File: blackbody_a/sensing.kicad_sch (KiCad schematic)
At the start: 3 parts, among them J1 Conn_02x03_Counter_Clockwise

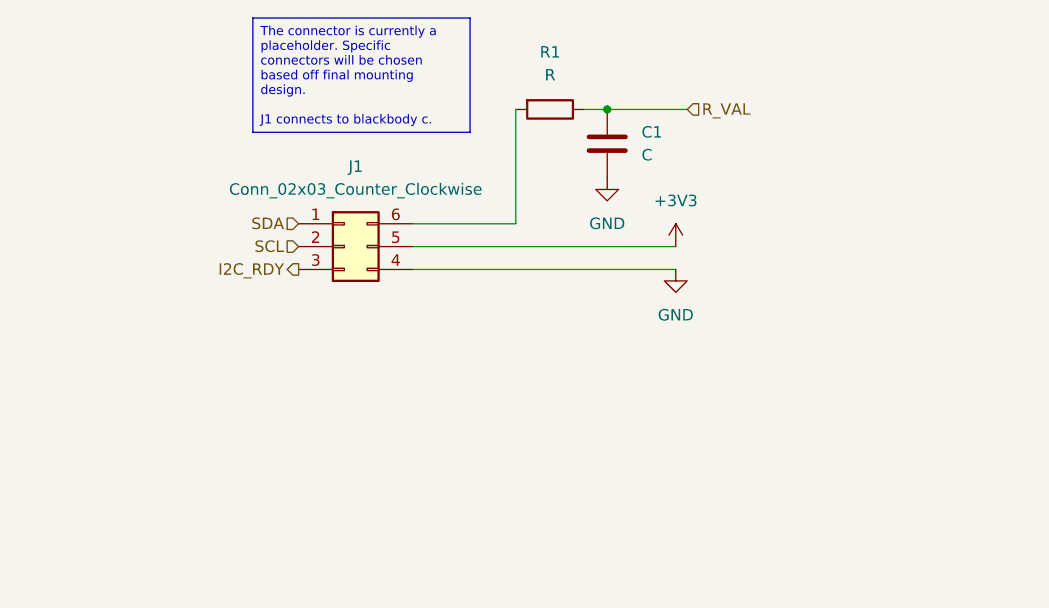
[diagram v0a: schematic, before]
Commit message: Initial version of sensor communication through all three boards
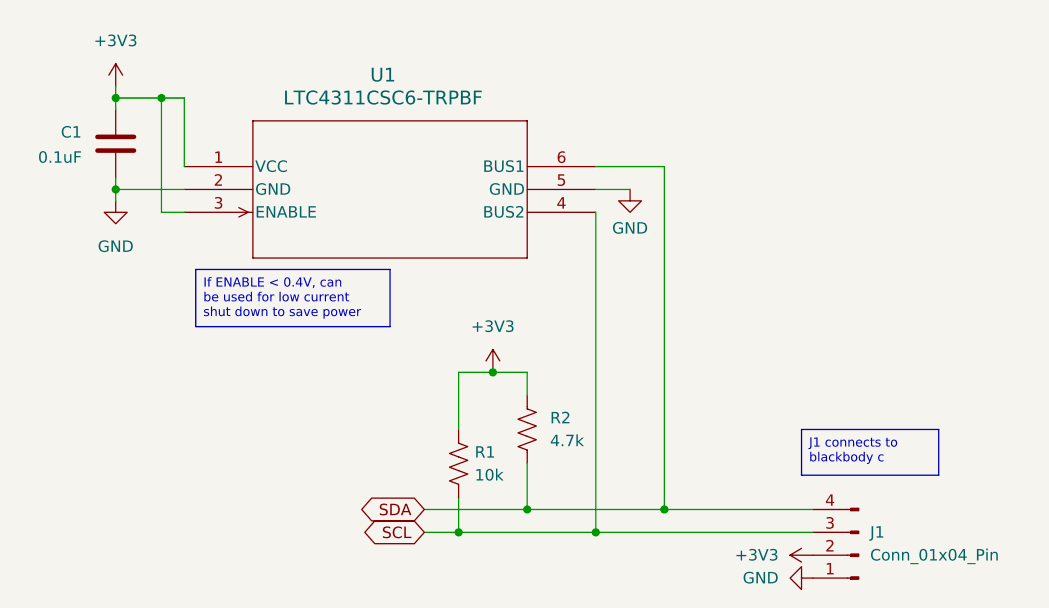
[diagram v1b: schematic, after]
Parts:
- removed J1: Conn_02x03_Counter_Clockwise, symbol Connector_Generic:Conn_02x03_Counter_Clockwise
- removed R1: R, symbol Device:R
- added J1: Conn_01x04_Pin, symbol Connector:Conn_01x04_Pin
- added R1: 10k, symbol Device:R_US
- added R2: 4.7k, symbol Device:R_US
- added U1: LTC4311CSC6-TRPBF, SOT-6_SC_LIT, symbol LTC4311:LTC4311CSC6-TRPBF
- C1: value C -> 0.1uF
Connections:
- net R_VAL is gone; now on net GND: C1.1
- net +3V3: now also C1.2, J1.2 (Pin_2), R1.1, R2.1, U1.1 (VCC), U1.3 (ENABLE)
- net GND: now also J1.1 (Pin_1), U1.2 (GND), U1.5 (GND); no longer C1.2
- net SCL: now also J1.3 (Pin_3), R1.2, U1.4 (BUS2)
- net SDA: now also J1.4 (Pin_4), R2.2, U1.6 (BUS1)

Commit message: Updated minor errors
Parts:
- R1: value 10k -> 4.7k
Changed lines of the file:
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@@
 			)
 		)
-		(property "Value" "10k"
+		(property "Value" "4.7k"
 			(at 116.078 93.98 0)
 			(effects

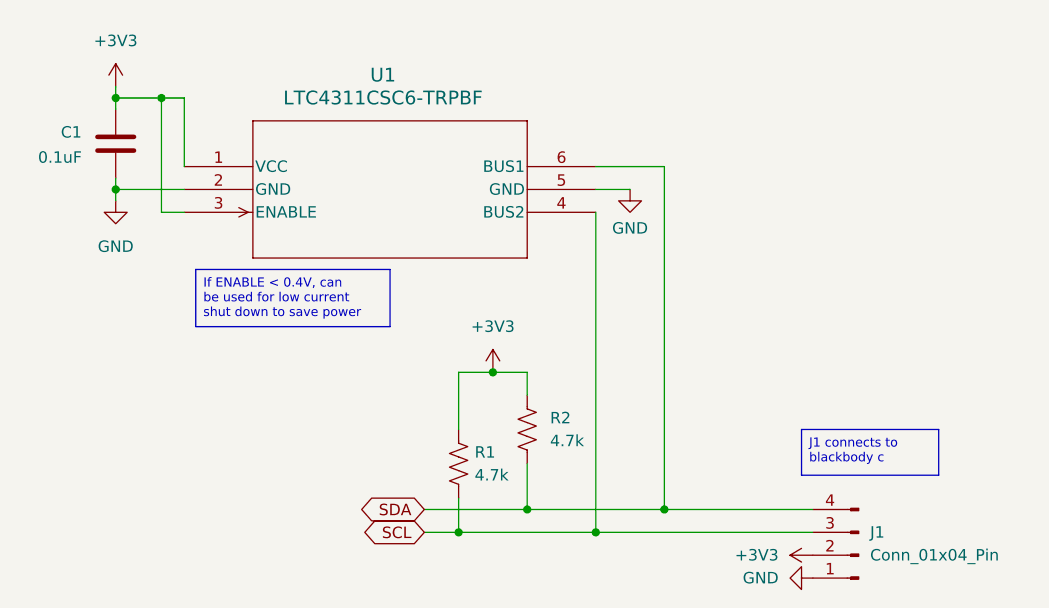
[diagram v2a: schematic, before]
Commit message: Added power distribution
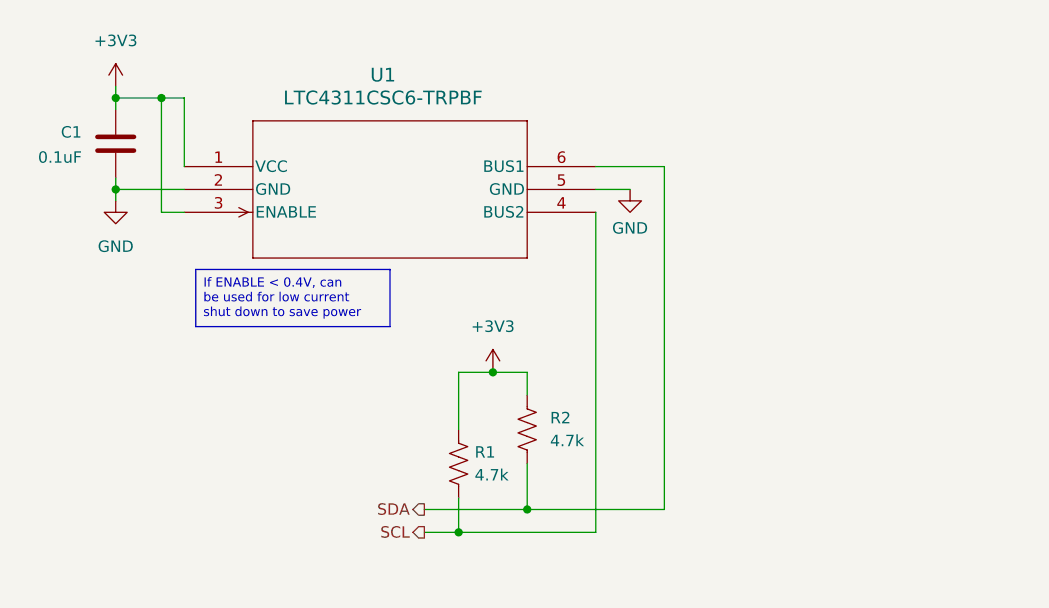
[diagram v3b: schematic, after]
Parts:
- removed J1: Conn_01x04_Pin, symbol Connector:Conn_01x04_Pin

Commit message: layout iteration 1
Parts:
- C1: footprint (none) -> Capacitor_SMD:C_0805_2012Metric
- R1, R2: footprint (none) -> Resistor_SMD:R_0805_2012Metric
- U1: footprint SOT-6_SC_LIT -> blackbody_a:SOT-6_SC_LIT
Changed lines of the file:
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@@
 (kicad_sch
-	(version 20231120)
+	(version 20250114)
 	(generator "eeschema")
-	(generator_version "8.0")
+	(generator_version "9.0")
 	(paper "A4")
+	(text_box "If ENABLE < 0.4V, can be used for low current shut down to save power"
+		(exclude_from_sim no)
+		(at 85.09 71.12 0)
+		(size 21.59 6.35)
+		(margins 0.762 0.762 0.762 0.762)
+		(stroke
+			(width 0)
+			(type default)
+		)
+		(fill
+			(type none)
+		)
+		(effects
+			(font
+				(size 1.016 1.016)
+			)
+			(justify left top)
+		)
+	)
 	(junction
 		(at 81.28 52.07)
@@
 		)
 	)
-	(text_box "If ENABLE < 0.4V, can be used for low current shut down to save power"
-		(exclude_from_sim no)
-		(at 85.09 71.12 0)
-		(size 21.59 6.35)
-		(stroke
-			(width 0)
-			(type default)
-		)
-		(fill
-			(type none)
-		)
-		(effects
-			(font
-				(size 1.016 1.016)
-			)
-			(justify left top)
-		)
-	)
 	(hierarchical_label "SCL"
 		(shape output)
 		(at 110.49 100.33 180)
-		(fields_autoplaced yes)
 		(effects
 			(font
@@
 		(shape output)
 		(at 110.49 97.79 180)
-		(fields_autoplaced yes)
 		(effects
 			(font
@@
 			)
 		)
-		(property "Footprint" ""
+		(property "Footprint" "Resistor_SMD:R_0805_2012Metric"
 			(at 115.316 92.964 90)
 			(effects
@@
 			)
 		)
-		(property "Footprint" "SOT-6_SC_LIT"
+		(property "Footprint" "blackbody_a:SOT-6_SC_LIT"
 			(at 83.82 59.69 0)
 			(effects
@@
 			)
 		)
-		(property "Footprint" ""
+		(property "Footprint" "Resistor_SMD:R_0805_2012Metric"
 			(at 122.936 89.154 90)
 			(effects
@@
 			)
 		)
-		(property "Footprint" ""
+		(property "Footprint" "Capacitor_SMD:C_0805_2012Metric"
 			(at 75.2348 53.34 0)
 			(effects

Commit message: layout edits
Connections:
- net +3V3 renamed +3.3V
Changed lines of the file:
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@@
+	)
+	(junction
+		(at 118.11 82.55)
+		(diameter 0)
+		(color 0 0 0 0)
 	)
 	(junction
@@
 		(color 0 0 0 0)
 	)
-	(junction
-		(at 118.11 82.55)
-		(diameter 0)
-		(color 0 0 0 0)
-	)
 	(wire
 		(pts
@@
 	(wire
 		(pts
+			(xy 81.28 64.77) (xy 81.28 52.07)
+		)
+		(stroke
+			(width 0)
+			(type default)
+		)
+	)
+	(wire
+		(pts
+			(xy 110.49 100.33) (xy 114.3 100.33)
+		)
+		(stroke
+			(width 0)
+			(type default)
+		)
+	)
+	(wire
+		(pts
+			(xy 121.92 82.55) (xy 121.92 85.09)
+		)
+		(stroke
+			(width 0)
+			(type default)
+		)
+	)
+	(wire
+		(pts
+			(xy 129.54 59.69) (xy 137.16 59.69)
+		)
+		(stroke
+			(width 0)
+			(type default)
+		)
+	)
+	(wire
+		(pts
+			(xy 76.2 52.07) (xy 76.2 53.34)
+		)
+		(stroke
+			(width 0)
+			(type default)
+		)
+	)
+	(wire
+		(pts
+			(xy 83.82 64.77) (xy 81.28 64.77)
+		)
+		(stroke
+			(width 0)
+			(type default)
+		)
+	)
+	(wire
+		(pts
+			(xy 137.16 59.69) (xy 137.16 97.79)
+		)
+		(stroke
+			(width 0)
+			(type default)
+		)
+	)
+	(wire
+		(pts
+			(xy 76.2 52.07) (xy 81.28 52.07)
+		)
+		(stroke
+			(width 0)
+			(type default)
+		)
+	)
+	(wire
+		(pts
+			(xy 114.3 82.55) (xy 118.11 82.55)
+		)
+		(stroke
+			(width 0)
+			(type default)
+		)
+	)
+	(wire
+		(pts
+			(xy 83.82 52.07) (xy 83.82 59.69)
+		)
+		(stroke
+			(width 0)
+			(type default)
+		)
+	)
+	(wire
+		(pts
+			(xy 76.2 62.23) (xy 83.82 62.23)
+		)
+		(stroke
+			(width 0)
+			(type default)
+		)
+	)
+	(wire
+		(pts
+			(xy 114.3 100.33) (xy 129.54 100.33)
+		)
+		(stroke
+			(width 0)
+			(type default)
+		)
+	)
+	(wire
+		(pts
+			(xy 81.28 52.07) (xy 83.82 52.07)
+		)
+		(stroke
+			(width 0)
+			(type default)
+		)
+	)
+	(wire
+		(pts
+			(xy 121.92 92.71) (xy 121.92 97.79)
+		)
+		(stroke
+			(width 0)
+			(type default)
+		)
+	)
+	(wire
+		(pts
 			(xy 118.11 82.55) (xy 121.92 82.55)
-		)
-		(stroke
-			(width 0)
-			(type default)
-		)
-	)
-	(wire
-		(pts
-			(xy 81.28 64.77) (xy 81.28 52.07)
-		)
-		(stroke
-			(width 0)
-			(type default)
-		)
-	)
-	(wire
-		(pts
-			(xy 110.49 100.33) (xy 114.3 100.33)
-		)
-		(stroke
-			(width 0)
-			(type default)
-		)
-	)
-	(wire
-		(pts
-			(xy 121.92 82.55) (xy 121.92 85.09)
-		)
-		(stroke
-			(width 0)
-			(type default)
-		)
-	)
-	(wire
-		(pts
-			(xy 129.54 59.69) (xy 137.16 59.69)
-		)
-		(stroke
-			(width 0)
-			(type default)
-		)
-	)
-	(wire
-		(pts
-			(xy 76.2 52.07) (xy 76.2 53.34)
-		)
-		(stroke
-			(width 0)
-			(type default)
-		)
-	)
-	(wire
-		(pts
-			(xy 83.82 64.77) (xy 81.28 64.77)
-		)
-		(stroke
-			(width 0)
-			(type default)
-		)
-	)
-	(wire
-		(pts
-			(xy 137.16 59.69) (xy 137.16 97.79)
-		)
-		(stroke
-			(width 0)
-			(type default)
-		)
-	)
-	(wire
-		(pts
-			(xy 76.2 52.07) (xy 81.28 52.07)
-		)
-		(stroke
-			(width 0)
-			(type default)
-		)
-	)
-	(wire
-		(pts
-			(xy 114.3 82.55) (xy 118.11 82.55)
-		)
-		(stroke
-			(width 0)
-			(type default)
-		)
-	)
-	(wire
-		(pts
-			(xy 83.82 52.07) (xy 83.82 59.69)
-		)
-		(stroke
-			(width 0)
-			(type default)
-		)
-	)
-	(wire
-		(pts
-			(xy 76.2 62.23) (xy 83.82 62.23)
-		)
-		(stroke
-			(width 0)
-			(type default)
-		)
-	)
-	(wire
-		(pts
-			(xy 114.3 100.33) (xy 129.54 100.33)
-		)
-		(stroke
-			(width 0)
-			(type default)
-		)
-	)
-	(wire
-		(pts
-			(xy 81.28 52.07) (xy 83.82 52.07)
-		)
-		(stroke
-			(width 0)
-			(type default)
-		)
-	)
-	(wire
-		(pts
-			(xy 121.92 92.71) (xy 121.92 97.79)
 		)
 		(stroke
@@
 	)
 	(symbol
-		(lib_id "power:+3V3")
-		(at 76.2 50.8 0)
-		(unit 1)
-		(exclude_from_sim no)
-		(in_bom yes)
-		(on_board yes)
-		(dnp no)
-		(fields_autoplaced yes)
-		(property "Reference" "#PWR02"
-			(at 76.2 54.61 0)
-			(effects
-				(font
-					(size 1.27 1.27)
-				)
-				(hide yes)
-			)
-		)
-		(property "Value" "+3V3"
-			(at 76.2 45.72 0)
-			(effects
-				(font
-					(size 1.27 1.27)
-				)
-			)
-		)
-		(property "Footprint" ""
-			(at 76.2 50.8 0)
-			(effects
-				(font
-					(size 1.27 1.27)
-				)
-				(hide yes)
-			)
-		)
-		(property "Datasheet" ""
-			(at 76.2 50.8 0)
-			(effects
-				(font
-					(size 1.27 1.27)
-				)
-				(hide yes)
-			)
-		)
-		(property "Description" "Power symbol creates a global label with name \"+3V3\""
-			(at 76.2 50.8 0)
-			(effects
-				(font
-					(size 1.27 1.27)
-				)
-				(hide yes)
-			)
-		)
-		(pin "1"
-		)
-		(instances
-			(project "blackbody_a"
-				(path "/1fc8ae43-742a-46b6-a93b-79253d0d0202/23416f09-d335-4c4f-b453-076ae86ec0b4"
-					(reference "#PWR02")
-					(unit 1)
-				)
-			)
-		)
-	)
-	(symbol
 		(lib_id "power:GND")
 		(at 133.35 62.23 0)
@@
 	)
 	(symbol
-		(lib_id "power:+3V3")
+		(lib_id "power:+3.3V")
 		(at 118.11 82.55 0)
 		(unit 1)
@@
 		(dnp no)
 		(fields_autoplaced yes)
-		(property "Reference" "#PWR04"
+		(property "Reference" "#PWR035"
 			(at 118.11 86.36 0)
 			(effects
@@
 			)
 		)
-		(property "Value" "+3V3"
+		(property "Value" "+3.3V"
 			(at 118.11 77.47 0)
 			(effects
@@
 			)
 		)
-		(property "Description" "Power symbol creates a global label with name \"+3V3\""
+		(property "Description" "Power symbol creates a global label with name \"+3.3V\""
 			(at 118.11 82.55 0)
 			(effects
@@
 			(project "blackbody_a"
 				(path "/1fc8ae43-742a-46b6-a93b-79253d0d0202/23416f09-d335-4c4f-b453-076ae86ec0b4"
-					(reference "#PWR04")
+					(reference "#PWR035")
 					(unit 1)
 				)
@@
 					(unit 1)
 				)
+			)
+		)
+	)
+	(symbol
+		(lib_id "power:+3.3V")
+		(at 76.2 50.8 0)
+		(unit 1)
+		(exclude_from_sim no)
+		(in_bom yes)
+		(on_board yes)
+		(dnp no)
+		(fields_autoplaced yes)
+		(property "Reference" "#PWR040"
+			(at 76.2 54.61 0)
+			(effects
+				(font
+					(size 1.27 1.27)
+				)
+				(hide yes)
+			)
+		)
+		(property "Value" "+3.3V"
+			(at 76.2 45.72 0)
+			(effects
+				(font
+					(size 1.27 1.27)
+				)
+			)
+		)
+		(property "Footprint" ""
+			(at 76.2 50.8 0)
+			(effects
+				(font
+					(size 1.27 1.27)
+				)
+				(hide yes)
+			)
+		)
+		(property "Datasheet" ""
+			(at 76.2 50.8 0)
+			(effects
+				(font
+					(size 1.27 1.27)
+				)
+				(hide yes)
+			)
+		)
+		(property "Description" "Power symbol creates a global label with name \"+3.3V\""
+			(at 76.2 50.8 0)
+			(effects
+				(font
+					(size 1.27 1.27)
+				)
+				(hide yes)
+			)
+		)
+		(pin "1"
+		)
+		(instances
+			(project "blackbody_a"
+				(path "/1fc8ae43-742a-46b6-a93b-79253d0d0202/23416f09-d335-4c4f-b453-076ae86ec0b4"
+					(reference "#PWR040")
+					(unit 1)
+				)

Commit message: layout updates
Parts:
- C1: Manufacturer_Part_Number (none) -> C0805C104M5R; Mouser Part Number (none) -> 80-C0805C104M5R; PN (none) -> C0805C104M5RACTU
- R1, R2: Mouser Part Number (none) -> 603-RT0805FRE074K7L; PN (none) -> RT0805FRE074K7L
- U1: Mouser Part Number (none) -> 584-LTC4311CSC6TRPBF; PN (none) -> LTC4311CSC6TRPBF
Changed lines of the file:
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@@
+			)
+		)
+		(property "Mouser Part Number" "603-RT0805FRE074K7L "
+			(at 114.3 92.71 0)
+			(effects
+				(font
+					(size 1.27 1.27)
+				)
+			)
+		)
+		(property "PN" "RT0805FRE074K7L"
+			(at 114.3 92.71 0)
+			(effects
+				(font
+					(size 1.27 1.27)
+				)
 			)
 		)
@@
 			)
 		)
+		(property "Mouser Part Number" "584-LTC4311CSC6TRPBF"
+			(at 83.82 59.69 0)
+			(effects
+				(font
+					(size 1.27 1.27)
+				)
+			)
+		)
+		(property "PN" "LTC4311CSC6TRPBF"
+			(at 83.82 59.69 0)
+			(effects
+				(font
+					(size 1.27 1.27)
+				)
+			)
+		)
 		(pin "1"
 		)
@@
 			)
 		)
+		(property "Mouser Part Number" "603-RT0805FRE074K7L "
+			(at 121.92 88.9 0)
+			(effects
+				(font
+					(size 1.27 1.27)
+				)
+			)
+		)
+		(property "PN" "RT0805FRE074K7L"
+			(at 121.92 88.9 0)
+			(effects
+				(font
+					(size 1.27 1.27)
+				)
+			)
+		)
 		(pin "2"
 		)
@@
 			)
 		)
+		(property "Manufacturer_Part_Number" "C0805C104M5R"
+			(at 76.2 57.15 0)
+			(effects
+				(font
+					(size 1.27 1.27)
+				)
+			)
+		)
+		(property "Mouser Part Number" "80-C0805C104M5R"
+			(at 76.2 57.15 0)
+			(effects
+				(font
+					(size 1.27 1.27)
+				)
+			)
+		)
+		(property "PN" "C0805C104M5RACTU"
+			(at 76.2 57.15 0)
+			(effects
+				(font
+					(size 1.27 1.27)
+				)
+			)
+		)
